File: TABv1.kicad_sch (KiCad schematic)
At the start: 27 parts, among them J10 Conn_UART_HOST, J11 Conn_UART_1, J12 Conn_UART_0, J13 Conn_ADC, J6 Conn_01x03_Pin, J8 Conn_SPI1, J9 Conn_SPI0, SW2 RESET, U1 RP2350B-QFN80, Y1 12MHz

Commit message: bozza layout pcb
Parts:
- added H1, H2, H3, H4: MountingHole, MountingHole:MountingHole_2.2mm_M2, symbol Mechanical:MountingHole
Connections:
- net MAG_CS: now reaches U1.12 (GPIO13)
- net IMU45_INT1: now reaches U1.18 (GPIO18)
- net IMU45_INT2: now reaches U1.19 (GPIO19)
- net IMU45_CS: now reaches U1.9 (GPIO11)
- net +3.3V renamed +3V3
- no-connect marks 9 -> 5
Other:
- sheet Sensors ports: added IMU45_CS, IMU45_INT1, IMU45_INT2, MAG_CS; removed none

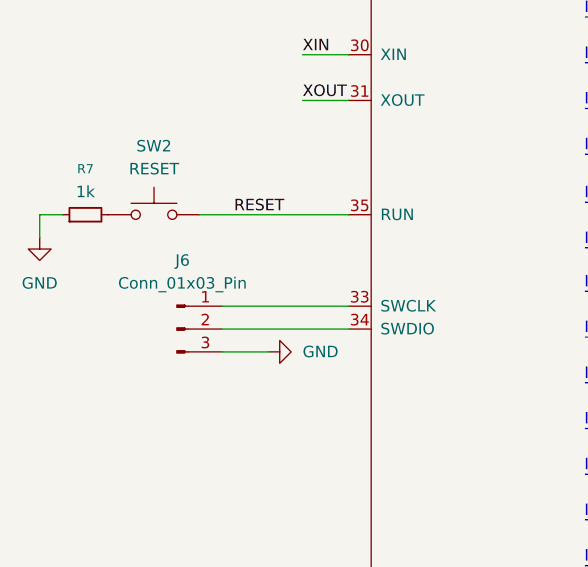
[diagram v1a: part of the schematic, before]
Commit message: ridimensionamento scheda
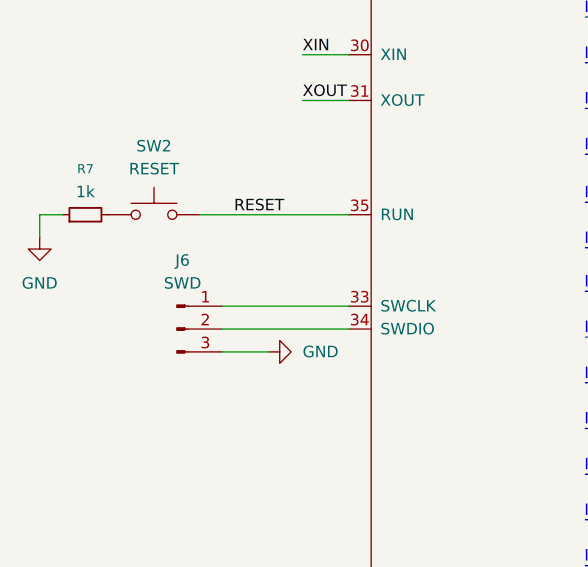
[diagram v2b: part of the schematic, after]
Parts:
- J6: value Conn_01x03_Pin -> SWD
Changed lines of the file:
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@@
 			)
 		)
-		(property "Value" "Conn_01x03_Pin"
+		(property "Value" "SWD"
 			(at 37.465 119.38 0)
 			(effects

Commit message: inserimento servo
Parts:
- added J2, J3: Conn_02x03_Row_Letter_Last, Connector_PinHeader_2.54mm:PinHeader_2x03_P2.54mm_Horizontal, symbol Connector_Generic:Conn_02x03_Row_Letter_Last
- H1, H2, H3, H4: now in the parts list
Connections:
- net GND: now also J2.3a (Pin_3a), J2.3b (Pin_3b), J3.3a (Pin_3a), J3.3b (Pin_3b)
- net PWM1: now reaches J9.4 (Pin_4), U1.20 (GPIO20)
- net PWM1: now also J2.1b (Pin_1b)
- net PWM2: now reaches J9.3 (Pin_3), U1.21 (GPIO21)
- net PWM2: now also J2.1a (Pin_1a)
- net PWM3: now reaches J9.2 (Pin_2), U1.22 (GPIO22)
- net PWM3: now also J3.1b (Pin_1b)
- net PWM4: now reaches J9.1 (Pin_1), U1.23 (GPIO23)
- net PWM4: now also J3.1a (Pin_1a)
- new net +BATT: J2.2a (Pin_2a), J2.2b (Pin_2b), J3.2a (Pin_2a), J3.2b (Pin_2b)
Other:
- moved on the sheet: H2, J9

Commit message: led e buzzer
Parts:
- added D5: BLUE, LED_SMD:LED_0603_1608Metric, symbol Device:LED_Small
- added D6: GREEN, LED_SMD:LED_0603_1608Metric, symbol Device:LED_Small
- added D7: RED, LED_SMD:LED_0603_1608Metric, symbol Device:LED_Small
- added LS1: CMT-8503-85B-SMT-TR, CMT-8503-85B-SMT-TR:XDCR_CMT-8503-85B-SMT-TR, symbol CMT-8503-85B-SMT-TR:CMT-8503-85B-SMT-TR
- added Q2: NMOS, Package_TO_SOT_SMD:SOT-23, symbol Simulation_SPICE:NMOS
- added R10: 100, Resistor_SMD:R_0603_1608Metric_Pad0.98x0.95mm_HandSolder, symbol Device:R_Small
- added R11: 10K, Resistor_SMD:R_0603_1608Metric_Pad0.98x0.95mm_HandSolder, symbol Device:R_Small
- added RN10: 220 Ohm, Resistor_SMD:R_Array_Convex_4x0603, symbol Device:R_Pack04
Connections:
- net +3V3: now also LS1.P
- net GND: now also D5.1 (K), D6.1 (K), D7.1 (K), Q2.3 (S), R11.1
- net L_RED: now reaches U1.36 (GPIO28)
- net L_RED: now also RN10.3 (R3.1), RN10.4 (R4.1)
- net L_GREEN: now reaches U1.37 (GPIO29)
- net L_GREEN: now also RN10.2 (R2.1)
- net L_BLUE: now reaches U1.56 (GPIO45_ADC5)
- net L_BLUE: now also RN10.1 (R1.1)
- net BUZZ: now reaches U1.57 (GPIO46_ADC6)
- net BUZZ: now also R10.1, R11.2
- new net: D6.2 (A), RN10.7 (R2.2)
- new net: LS1.N, Q2.1 (D)
- new net: Q2.2 (G), R10.2
- new net: D7.2 (A), RN10.5 (R4.2), RN10.6 (R3.2)
- new net: D5.2 (A), RN10.8 (R1.2)
- no-connect marks 5 -> 1
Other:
- added sheet LoRa Module (loramodule.kicad_sch)
- moved on the sheet: C10, C11, C12, C13, C14, C15, C16, C17, C5, C6, C7, C8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

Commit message: footprint modulo radio
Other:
- removed sheet LoRa Module
- added sheet LoRa & GPS (loRa&GPS.kicad_sch)
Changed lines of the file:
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@@
+	)
+	(sheet
+		(at 143.51 232.41)
+		(size 54.61 44.45)
+		(exclude_from_sim no)
+		(in_bom yes)
+		(on_board yes)
+		(dnp no)
+		(fields_autoplaced yes)
+		(stroke
+			(width 0.1524)
+			(type solid)
+		)
+		(fill
+			(color 0 0 0 0.0000)
+		)
+		(property "Sheetname" "LoRa & GPS"
+			(at 143.51 231.6984 0)
+			(effects
+				(font
+					(size 1.27 1.27)
+				)
+				(justify left bottom)
+			)
+		)
+		(property "Sheetfile" "loRa&GPS.kicad_sch"
+			(at 143.51 277.4446 0)
+			(effects
+				(font
+					(size 1.27 1.27)
+				)
+				(justify left top)
+			)
+		)
+		(instances
+			(project "TABv1"
+				(path "/105f6e80-8e20-4d56-8eb3-6fa826818670"
+					(page "8")
+				)
+			)
+		)
 	)
 	(sheet
@@
 				)
 			)
-		)
-	)
-	(sheet
-		(at 246.38 201.93)
-		(size 31.75 26.67)
-		(exclude_from_sim no)
-		(in_bom yes)
-		(on_board yes)
-		(dnp no)
-		(fields_autoplaced yes)
-		(stroke
-			(width 0.1524)
-			(type solid)
-		)
-		(fill
-			(color 0 0 0 0.0000)
-		)
-		(property "Sheetname" "LoRa Module"
-			(at 246.38 201.2184 0)
-			(effects
-				(font
-					(size 1.27 1.27)
-				)
-				(justify left bottom)
-			)
-		)
-		(property "Sheetfile" "loramodule.kicad_sch"
-			(at 246.38 229.1846 0)
-			(effects
-				(font
-					(size 1.27 1.27)
-				)
-				(justify left top)
-			)
-		)
-		(instances
-			(project "TABv1"
-				(path "/105f6e80-8e20-4d56-8eb3-6fa826818670"
-					(page "7")
-				)
-			)

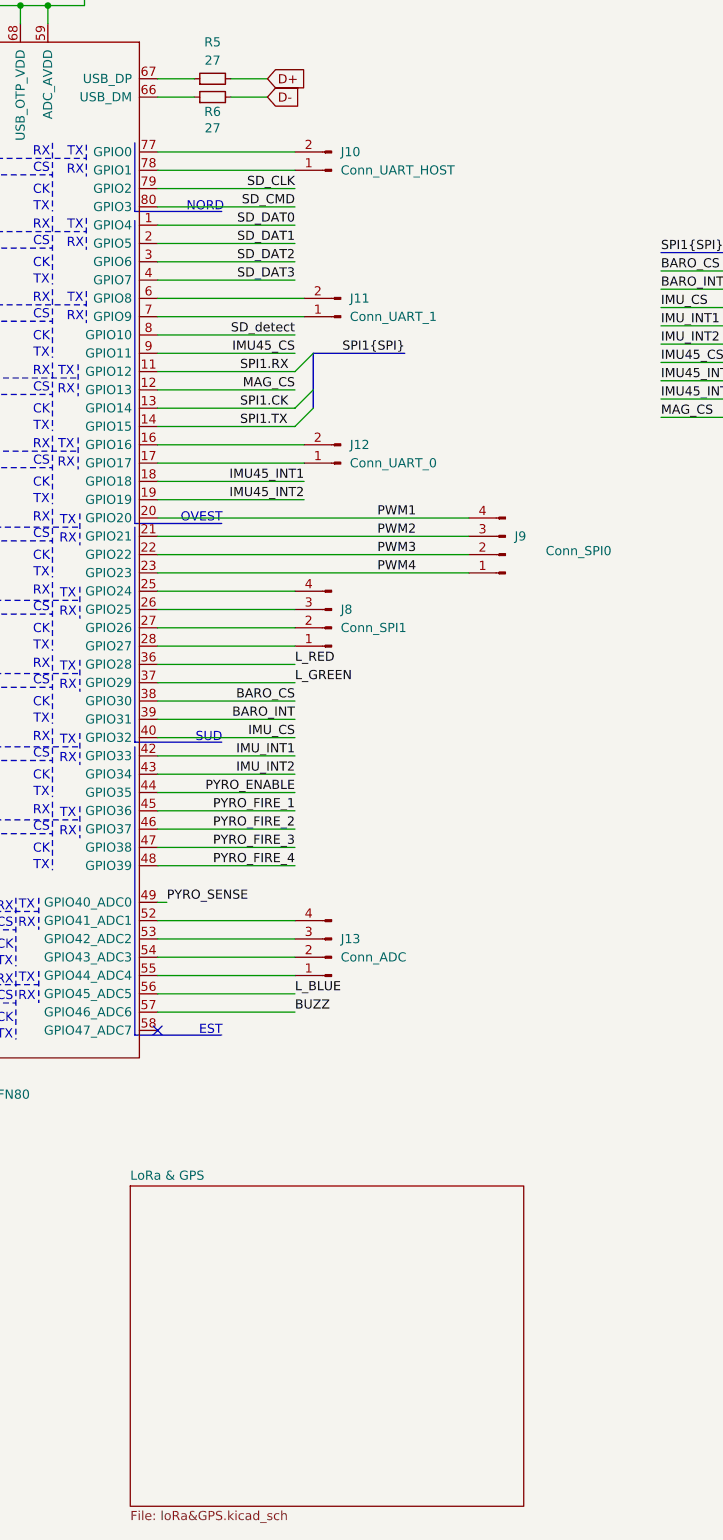
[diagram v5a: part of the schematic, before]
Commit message: Comunicazione Pico - GPS/Radio
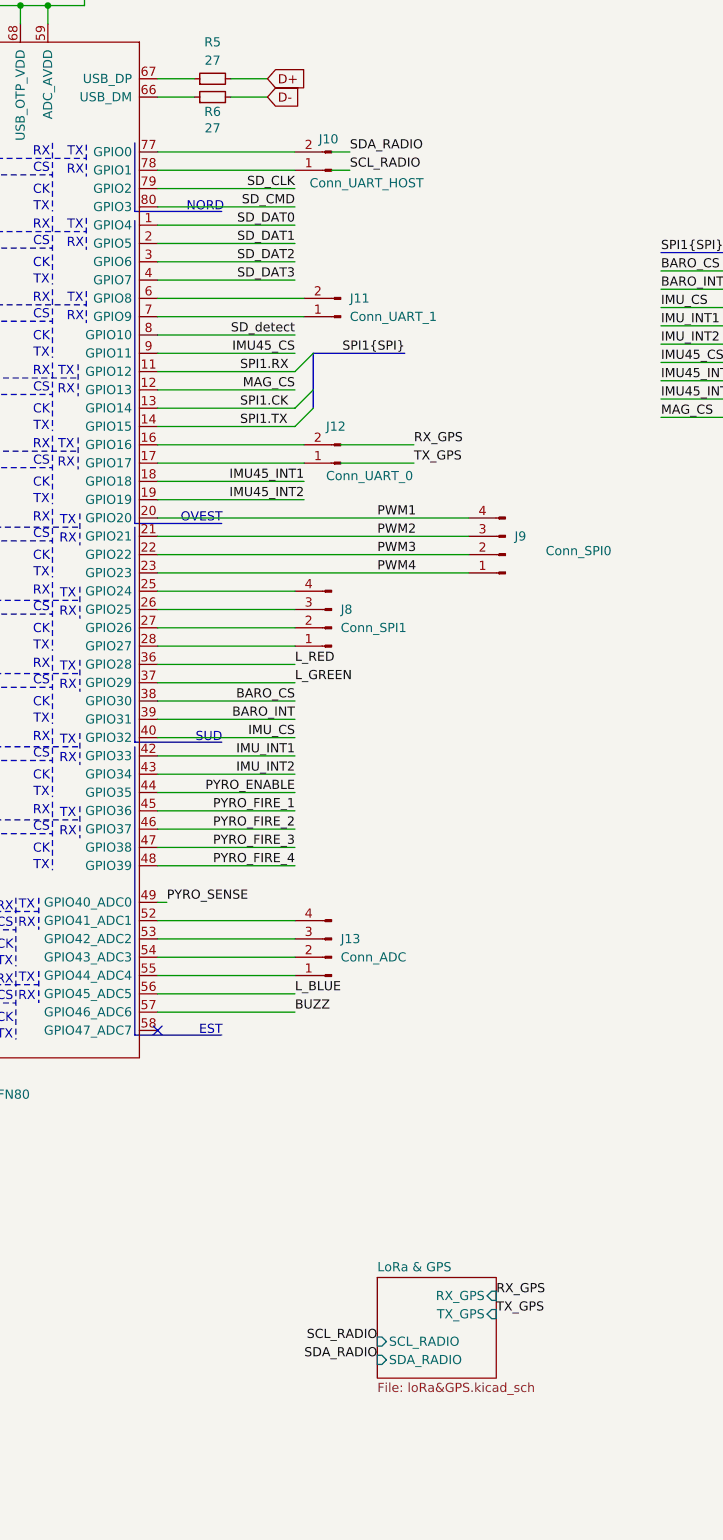
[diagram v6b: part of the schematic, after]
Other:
- sheet LoRa & GPS ports: added RX_GPS, SCL_RADIO, SDA_RADIO, TX_GPS; removed none
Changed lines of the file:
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@@
 	(wire
 		(pts
+			(xy 172.72 132.08) (xy 182.88 132.08)
+		)
+		(stroke
+			(width 0)
+			(type default)
+		)
+	)
+	(wire
+		(pts
 			(xy 217.17 123.19) (xy 232.41 123.19)
 		)
@@
 	(wire
 		(pts
+			(xy 172.72 129.54) (xy 182.88 129.54)
+		)
+		(stroke
+			(width 0)
+			(type default)
+		)
+	)
+	(wire
+		(pts
 			(xy 147.32 96.52) (xy 166.37 96.52)
 		)
@@
 	(wire
 		(pts
+			(xy 171.45 88.9) (xy 173.99 88.9)
+		)
+		(stroke
+			(width 0)
+			(type default)
+		)
+	)
+	(wire
+		(pts
 			(xy 342.9 87.63) (xy 345.44 87.63)
 		)
@@
 	(wire
 		(pts
+			(xy 171.45 91.44) (xy 173.99 91.44)
+		)
+		(stroke
+			(width 0)
+			(type default)
+		)
+	)
+	(wire
+		(pts
 			(xy 147.32 109.22) (xy 167.64 109.22)
 		)
@@
 		)
 	)
+	(label "TX_GPS"
+		(at 182.88 132.08 0)
+		(effects
+			(font
+				(size 1.27 1.27)
+			)
+			(justify left bottom)
+		)
+	)
 	(label "PYRO_FIRE_2"
 		(at 166.37 182.88 180)
@@
 		)
 	)
+	(label "RX_GPS"
+		(at 194.31 247.65 0)
+		(effects
+			(font
+				(size 1.27 1.27)
+			)
+			(justify left bottom)
+		)
+	)
 	(label "IMU_INT2"
 		(at 217.17 115.57 0)
@@
 		)
 	)
+	(label "SCL_RADIO"
+		(at 173.99 91.44 0)
+		(effects
+			(font
+				(size 1.27 1.27)
+			)
+			(justify left bottom)
+		)
+	)
 	(label "BARO_INT"
 		(at 217.17 107.95 0)
@@
 		)
 	)
+	(label "SCL_RADIO"
+		(at 177.8 254 180)
+		(effects
+			(font
+				(size 1.27 1.27)
+			)
+			(justify right bottom)
+		)
+	)
 	(label "SD2"
 		(at 57.15 107.95 0)
@@
 		)
 	)
+	(label "RX_GPS"
+		(at 182.88 129.54 0)
+		(effects
+			(font
+				(size 1.27 1.27)
+			)
+			(justify left bottom)
+		)
+	)
 	(label "SD_CMD"
 		(at 166.37 96.52 180)
@@
 		)
 	)
+	(label "TX_GPS"
+		(at 194.31 250.19 0)
+		(effects
+			(font
+				(size 1.27 1.27)
+			)
+			(justify left bottom)
+		)
+	)
 	(label "IMU45_CS"
 		(at 166.37 116.84 180)
@@
 		)
 	)
+	(label "SDA_RADIO"
+		(at 173.99 88.9 0)
+		(effects
+			(font
+				(size 1.27 1.27)
+			)
+			(justify left bottom)
+		)
+	)
 	(label "SD_DAT2"
 		(at 166.37 104.14 180)
@@
 		)
 	)
+	(label "SDA_RADIO"
+		(at 177.8 256.54 180)
+		(effects
+			(font
+				(size 1.27 1.27)
+			)
+			(justify right bottom)
+		)
+	)
 	(label "IMU_INT1"
 		(at 217.17 113.03 0)
@@
 		(on_board yes)
 		(dnp no)
-		(fields_autoplaced yes)
 		(property "Reference" "J12"
-			(at 173.99 129.5399 0)
+			(at 170.688 127 0)
 			(effects
 				(font
@@
 		)
 		(property "Value" "Conn_UART_0"
-			(at 173.99 132.0799 0)
+			(at 170.688 133.858 0)
 			(effects
 				(font
@@
 		(on_board yes)
 		(dnp no)
-		(fields_autoplaced yes)
 		(property "Reference" "J10"
-			(at 172.72 88.8999 0)
+			(at 169.672 87.122 0)
 			(effects
 				(font
@@
 		)
 		(property "Value" "Conn_UART_HOST"
-			(at 172.72 91.4399 0)
+			(at 168.402 93.218 0)
 			(effects
 				(font
@@
 	)
 	(sheet
-		(at 143.51 232.41)
-		(size 54.61 44.45)
+		(at 177.8 245.11)
+		(size 16.51 13.97)
 		(exclude_from_sim no)
 		(in_bom yes)
@@
 		)
 		(property "Sheetname" "LoRa & GPS"
-			(at 143.51 231.6984 0)
+			(at 177.8 244.3984 0)
 			(effects
 				(font
@@
 		)
 		(property "Sheetfile" "loRa&GPS.kicad_sch"
-			(at 143.51 277.4446 0)
+			(at 177.8 259.6646 0)
 			(effects
 				(font
@@
 			)
 		)
+		(pin "RX_GPS" input
+			(at 194.31 247.65 0)
+			(effects
+				(font
+					(size 1.27 1.27)
+				)
+				(justify right)
+			)
+		)
+		(pin "TX_GPS" input
+			(at 194.31 250.19 0)
+			(effects
+				(font
+					(size 1.27 1.27)
+				)
+				(justify right)
+			)
+		)
+		(pin "SCL_RADIO" input
+			(at 177.8 254 180)
+			(effects
+				(font
+					(size 1.27 1.27)
+				)
+				(justify left)
+			)
+		)
+		(pin "SDA_RADIO" input
+			(at 177.8 256.54 180)
+			(effects
+				(font
+					(size 1.27 1.27)
+				)
+				(justify left)
+			)
+		)

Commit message: Corrections
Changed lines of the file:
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@@
 	)
 	(junction
-		(at 351.79 194.31)
-		(diameter 0)
-		(color 0 0 0 0)
-	)
-	(junction
 		(at 336.55 237.49)
 		(diameter 0)
@@
 	)
 	(junction
+		(at 353.822 193.04)
+		(diameter 0)
+		(color 0 0 0 0)
+	)
+	(junction
 		(at 106.68 68.58)
 		(diameter 0)
@@
 	(wire
 		(pts
+			(xy 353.314 189.23) (xy 354.33 189.23)
+		)
+		(stroke
+			(width 0)
+			(type default)
+		)
+	)
+	(wire
+		(pts
 			(xy 217.17 107.95) (xy 232.41 107.95)
 		)
@@
 	(wire
 		(pts
+			(xy 352.806 193.04) (xy 353.822 193.04)
+		)
+		(stroke
+			(width 0)
+			(type default)
+		)
+	)
+	(wire
+		(pts
 			(xy 26.67 261.62) (xy 26.67 262.89)
 		)
@@
 	(wire
 		(pts
-			(xy 349.25 189.23) (xy 354.33 189.23)
-		)
-		(stroke
-			(width 0)
-			(type default)
-		)
-	)
-	(wire
-		(pts
 			(xy 55.88 85.09) (xy 77.47 85.09)
 		)
@@
 	(wire
 		(pts
-			(xy 346.71 194.31) (xy 351.79 194.31)
-		)
-		(stroke
-			(width 0)
-			(type default)
-		)
-	)
-	(wire
-		(pts
 			(xy 43.18 142.24) (xy 43.18 144.78)
 		)
@@
 		)
 	)
+	(wire
+		(pts
+			(xy 353.822 191.77) (xy 353.822 193.04)
+		)
+		(stroke
+			(width 0)
+			(type default)
+		)
+	)
 	(polyline
 		(pts
@@
 	(wire
 		(pts
-			(xy 351.79 194.31) (xy 354.33 194.31)
+			(xy 353.822 194.31) (xy 354.33 194.31)
 		)
 		(stroke
@@
 	(wire
 		(pts
-			(xy 354.33 191.77) (xy 351.79 191.77)
+			(xy 354.33 191.77) (xy 353.822 191.77)
 		)
 		(stroke
@@
 		)
 	)
-	(wire
-		(pts
-			(xy 347.98 186.69) (xy 354.33 186.69)
-		)
-		(stroke
-			(width 0)
-			(type default)
-		)
-	)
 	(polyline
 		(pts
@@
 	(wire
 		(pts
+			(xy 353.822 193.04) (xy 353.822 194.31)
+		)
+		(stroke
+			(width 0)
+			(type default)
+		)
+	)
+	(wire
+		(pts
 			(xy 147.32 96.52) (xy 166.37 96.52)
 		)
@@
 	(wire
 		(pts
-			(xy 347.98 189.23) (xy 347.98 186.69)
-		)
-		(stroke
-			(width 0)
-			(type default)
-		)
-	)
-	(wire
-		(pts
 			(xy 78.74 69.85) (xy 78.74 67.31)
 		)
@@
 		)
 	)
-	(wire
-		(pts
-			(xy 349.25 191.77) (xy 349.25 189.23)
-		)
-		(stroke
-			(width 0)
-			(type default)
-		)
-	)
 	(polyline
 		(pts
@@
 	(wire
 		(pts
-			(xy 346.71 189.23) (xy 347.98 189.23)
+			(xy 353.314 186.69) (xy 354.33 186.69)
 		)
 		(stroke
@@
 		)
 	)
-	(wire
-		(pts
-			(xy 351.79 191.77) (xy 351.79 194.31)
-		)
-		(stroke
-			(width 0)
-			(type default)
-		)
-	)
 	(bus
 		(pts
@@
 	(wire
 		(pts
-			(xy 346.71 191.77) (xy 349.25 191.77)
-		)
-		(stroke
-			(width 0)
-			(type default)
-		)
-	)
-	(wire
-		(pts
 			(xy 147.32 149.86) (xy 166.37 149.86)
 		)
@@
 	)
 	(label "L_GREEN"
-		(at 346.71 191.77 180)
+		(at 353.314 189.23 180)
 		(effects
 			(font
@@
 	)
 	(label "L_RED"
-		(at 346.71 194.31 180)
+		(at 352.806 193.04 180)
 		(effects
 			(font
@@
 	)
 	(label "L_BLUE"
-		(at 346.71 189.23 180)
+		(at 353.314 186.69 180)
 		(effects
 			(font

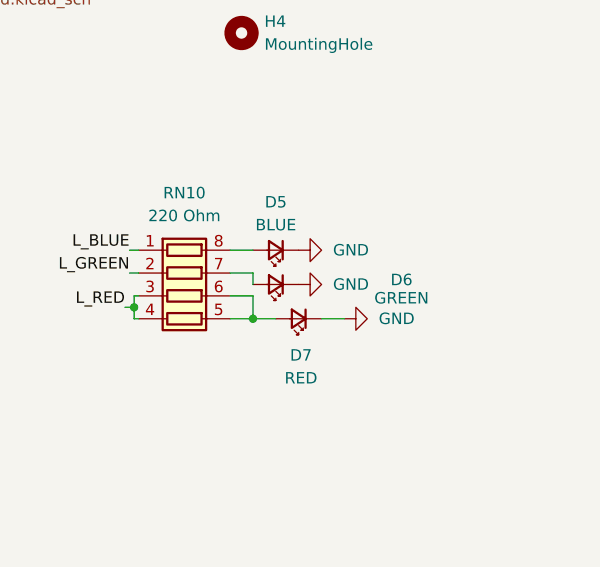
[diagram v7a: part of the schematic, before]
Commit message: RC-WLE5-434 aggiunta induttanza
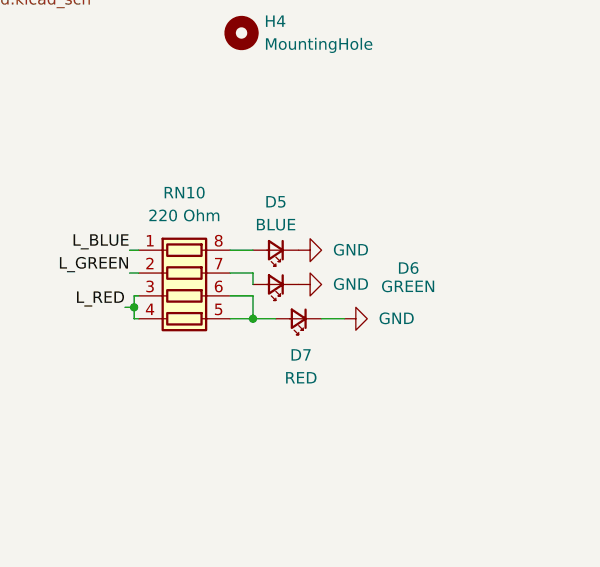
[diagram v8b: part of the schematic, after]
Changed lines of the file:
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@@
 		(dnp no)
 		(property "Reference" "D6"
-			(at 383.54 189.992 0)
+			(at 384.302 188.722 0)
 			(effects
 				(font
@@
 		)
 		(property "Value" "GREEN"
-			(at 383.54 192.024 0)
+			(at 384.302 190.754 0)
 			(effects
 				(font
